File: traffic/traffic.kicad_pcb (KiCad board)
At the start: 2 copper layers, 23.1 x 25.4 mm, 7 parts, among them J1 Conn_01x06_Male

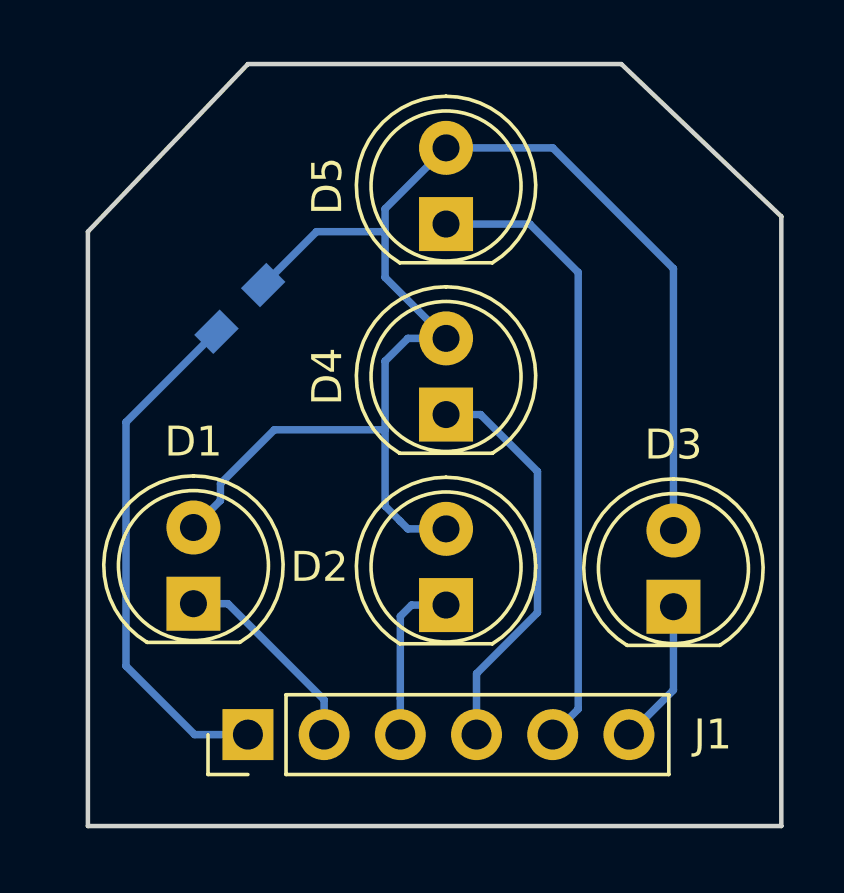
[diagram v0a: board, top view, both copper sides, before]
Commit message: labelled trafficLight module
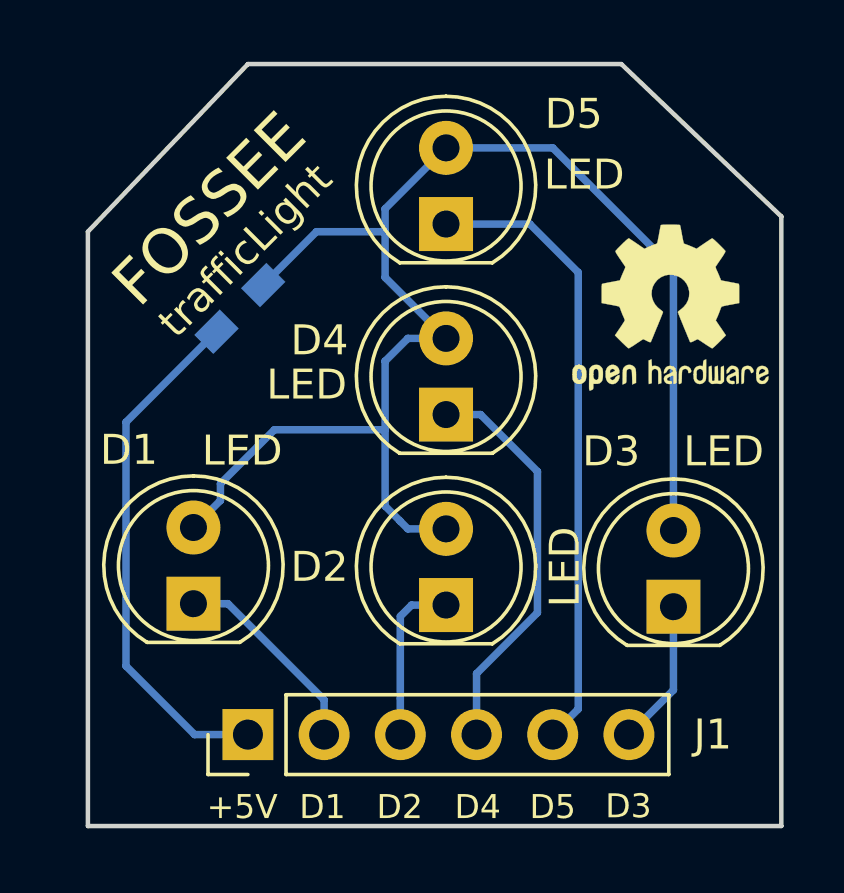
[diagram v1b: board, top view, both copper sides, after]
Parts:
- added REF***: OSHW-Logo2_7.3x6mm_SilkScreen, Symbols:OSHW-Logo2_7.3x6mm_SilkScreen, F.Cu at (154.8, 91.4)
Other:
- board text added: "+5V"
- board text added: "D1"
- board text added: "D2"
- board text added: "D3"
- board text added: "D4"
- board text added: "D5"
- board text added: "FOSSEE"
- board text added: "trafficLight"

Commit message: mounting holes in motor, extra pins in traffic, corrections in labels
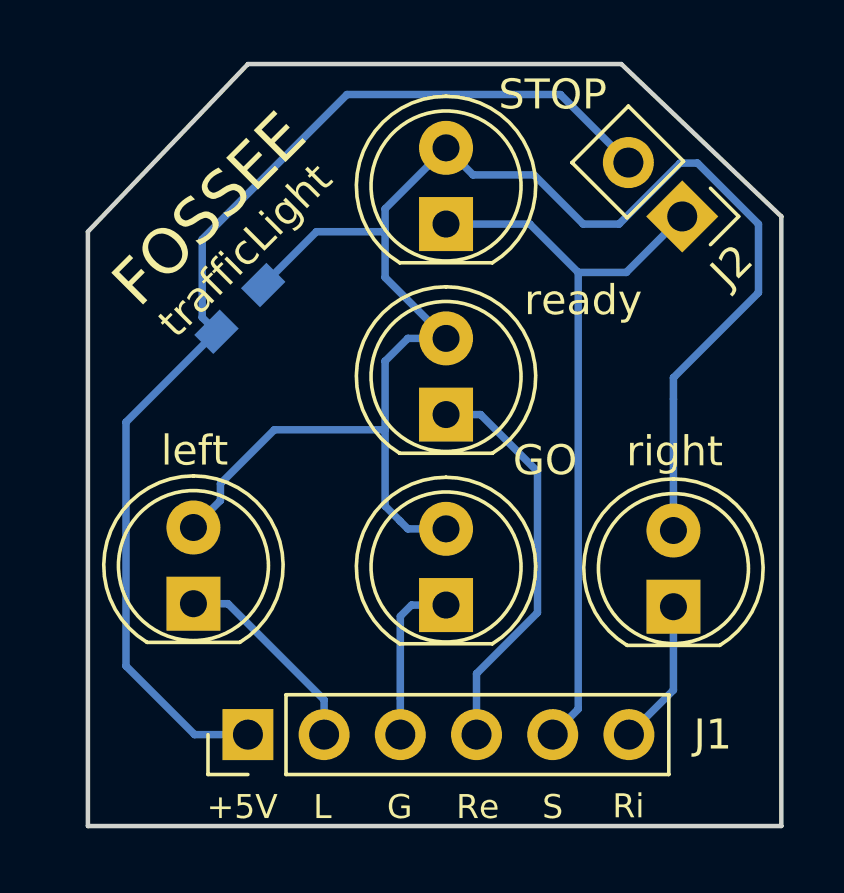
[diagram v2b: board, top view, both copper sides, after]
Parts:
- removed REF***: OSHW-Logo2_7.3x6mm_SilkScreen, Symbols:OSHW-Logo2_7.3x6mm_SilkScreen
- added J2: Conn_01x02_Male, Socket_Strips:Socket_Strip_Straight_1x02_Pitch2.54mm, F.Cu at (155.2, 88.4)
- D1: value LED -> left
- D2: value LED -> GO
- D3: value LED -> right
- D4: value LED -> ready
- D5: value LED -> STOP
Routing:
- net +5C: track 17.4 -> 37.8 mm
- net Net-(D1-Pad2): track 48.4 -> 55.0 mm
- net Net-(D5-Pad1): track 20.8 -> 25.1 mm
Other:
- board text added: "G"
- board text added: "L"
- board text added: "Re"
- board text added: "Ri"
- board text added: "S"
- board text removed: "D1"
- board text removed: "D2"
- board text removed: "D3"
- board text removed: "D4"
- board text removed: "D5"

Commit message: labels in trafficc
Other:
- board text added: "GND"
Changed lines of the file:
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@@
   (general
     (thickness 1.6)
-    (drawings 19)
+    (drawings 21)
     (tracks 58)
     (zones 0)
@@
       (effects (font (size 1 1) (thickness 0.15)))
     )
-    (fp_text value ready (at 3.81 4.572 180) (layer F.SilkS)
+    (fp_text value ready (at 3.81 4.318 180) (layer F.SilkS)
       (effects (font (size 1 1) (thickness 0.15)))
     )
@@
     )
   )
+  (gr_text GND (at 153.67 90.17 135) (layer F.SilkS)
+    (effects (font (size 0.8 0.8) (thickness 0.1)))
+  )
+  (gr_text +5V (at 151.892 88.392 135) (layer F.SilkS)
+    (effects (font (size 0.8 0.8) (thickness 0.1)))
+  )
   (dimension 12.446 (width 0.3) (layer Margin)

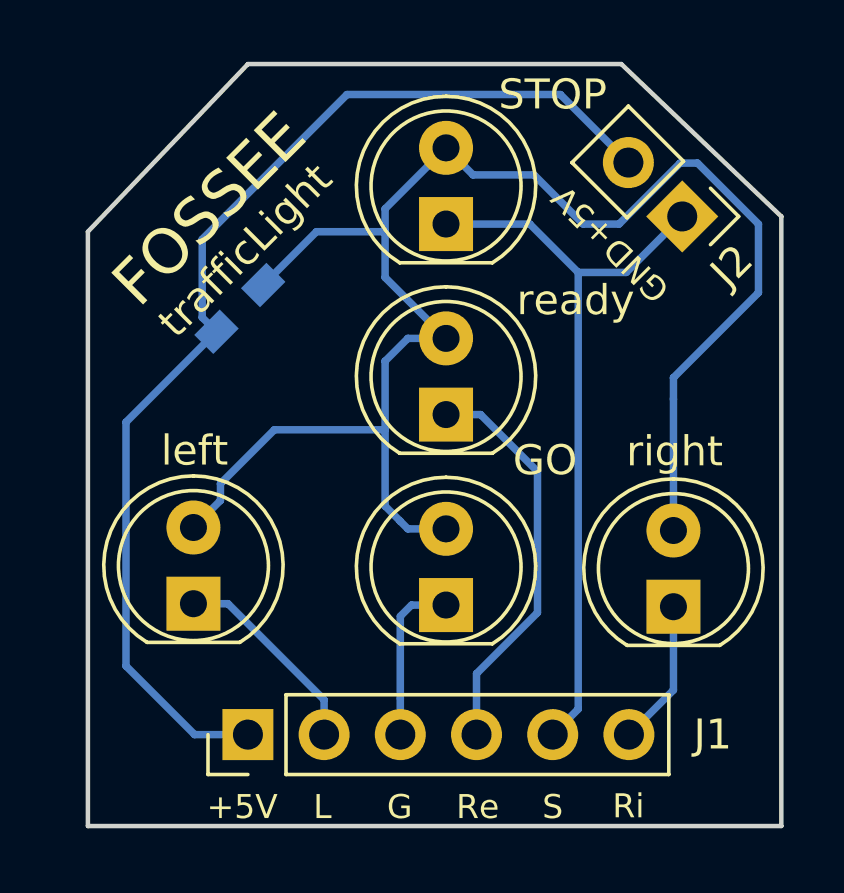
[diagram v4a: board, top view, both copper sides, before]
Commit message: transistor driving in traffic light; updated the BOM and gerbers accordingly
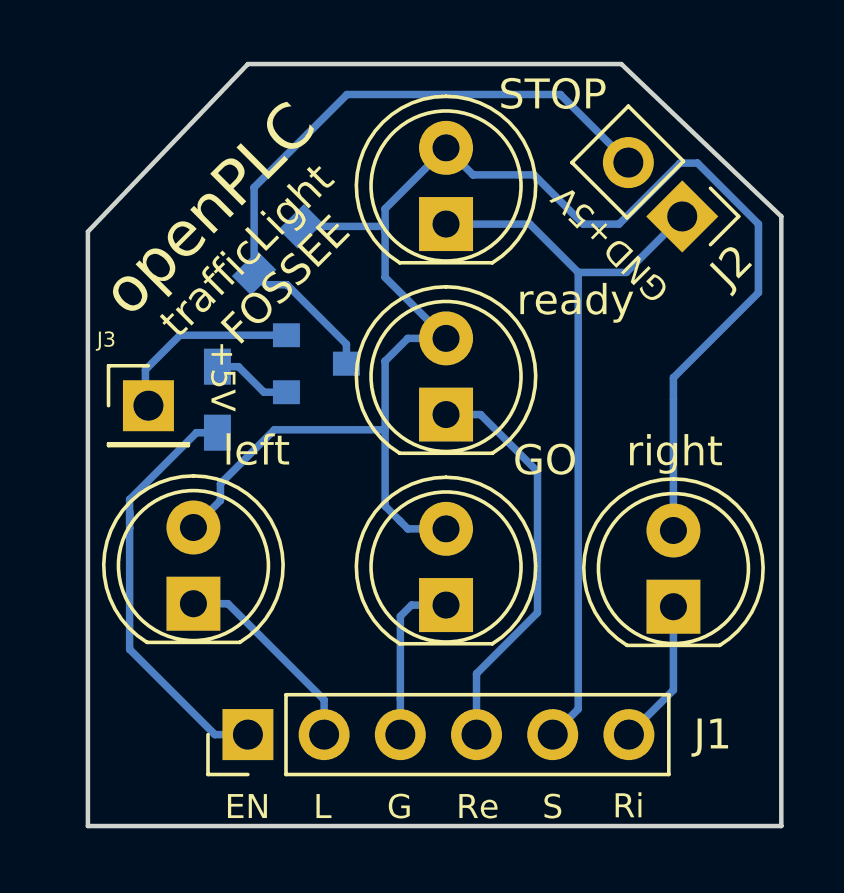
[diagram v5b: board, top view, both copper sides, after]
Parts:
- added J3: Conn_01x01_Male, Socket_Strips:Socket_Strip_Straight_1x01_Pitch2.54mm, F.Cu at (137.4, 94.7)
- added Q1: MMBT3906, TO_SOT_Packages_SMD:SOT-23, B.Cu at (143.0, 93.3)
- added R2: R, Resistors_SMD:R_0603_HandSoldering, B.Cu at (139.7, 94.5)
- moved R1 2.32 mm to (141.7, 89.5)
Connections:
- J1 pad 1: +5C -> Net-(J1-Pad1)
- J2 pad 2: +5C -> Net-(J2-Pad2)
- R1 pad 2: +5C -> Net-(J2-Pad2)
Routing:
- net +5C: track 37.8 -> 6.28 mm
- net Net-(J2-Pad2): track 0.00 -> 22.3 mm
- net Net-(J1-Pad1): track 0.00 -> 14.3 mm
- net Net-(Q1-Pad1): track 0.00 -> 2.65 mm
- net Net-(D1-Pad2): track 55.0 -> 53.0 mm
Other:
- board text added: "EN"
- board text added: "openPLC"
- board text added: "trafficLight FOSSEE"
- board text removed: "FOSSEE"
- board text removed: "trafficLight"
